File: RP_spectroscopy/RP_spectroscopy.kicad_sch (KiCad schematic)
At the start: 0 parts

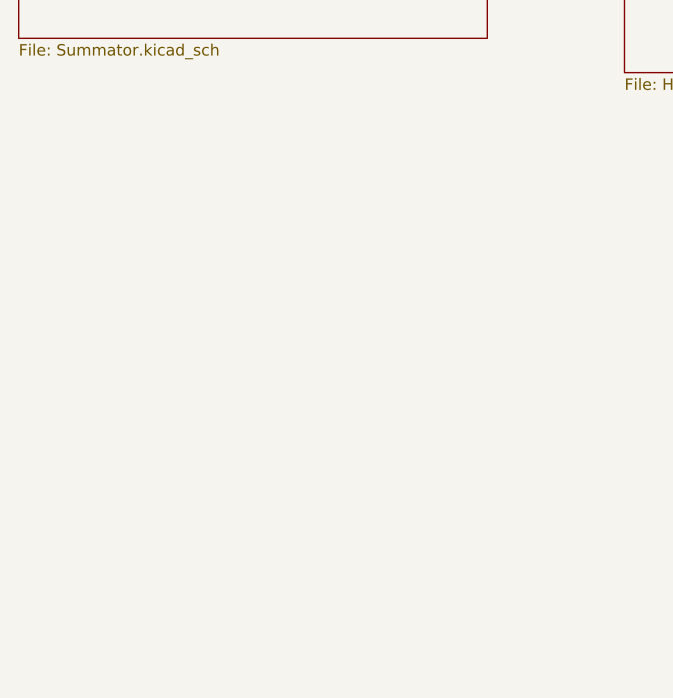
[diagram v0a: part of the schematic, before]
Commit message: Added the VCO schematic and started to draw it.
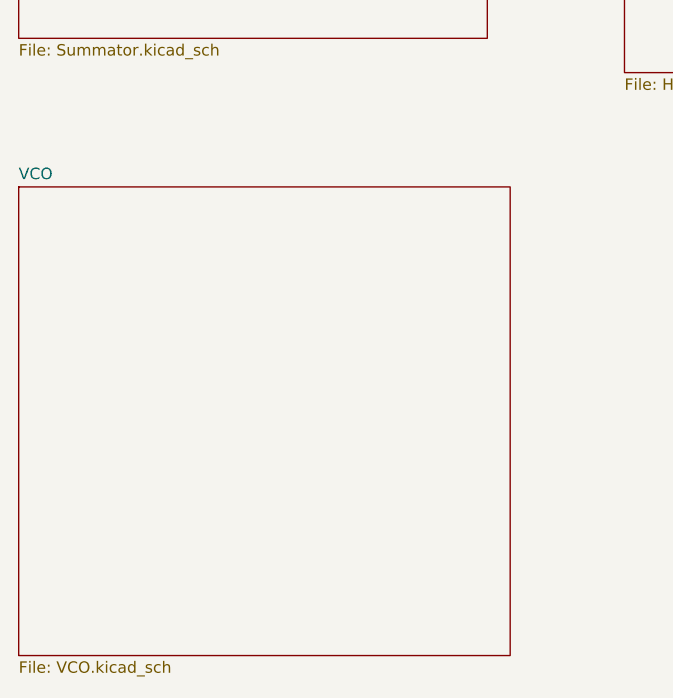
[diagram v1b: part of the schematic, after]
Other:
- added sheet VCO (VCO.kicad_sch)
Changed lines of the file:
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@@
+	)
+	(sheet
+		(at 21.59 88.9)
+		(size 54.61 52.07)
+		(exclude_from_sim no)
+		(in_bom yes)
+		(on_board yes)
+		(dnp no)
+		(fields_autoplaced yes)
+		(stroke
+			(width 0.1524)
+			(type solid)
+		)
+		(fill
+			(color 0 0 0 0.0000)
+		)
+		(property "Sheetname" "VCO"
+			(at 21.59 88.1884 0)
+			(effects
+				(font
+					(size 1.27 1.27)
+				)
+				(justify left bottom)
+			)
+		)
+		(property "Sheetfile" "VCO.kicad_sch"
+			(at 21.59 141.5546 0)
+			(effects
+				(font
+					(size 1.27 1.27)
+				)
+				(justify left top)
+			)
+		)
+		(instances
+			(project "RP_spectroscopy"
+				(path "/dd9ac3ef-6a3a-4df6-b083-1a4e73093ea8"
+					(page "6")
+				)
+			)
+		)
 	)
 	(sheet

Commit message: Deleted the VCO part from the main project
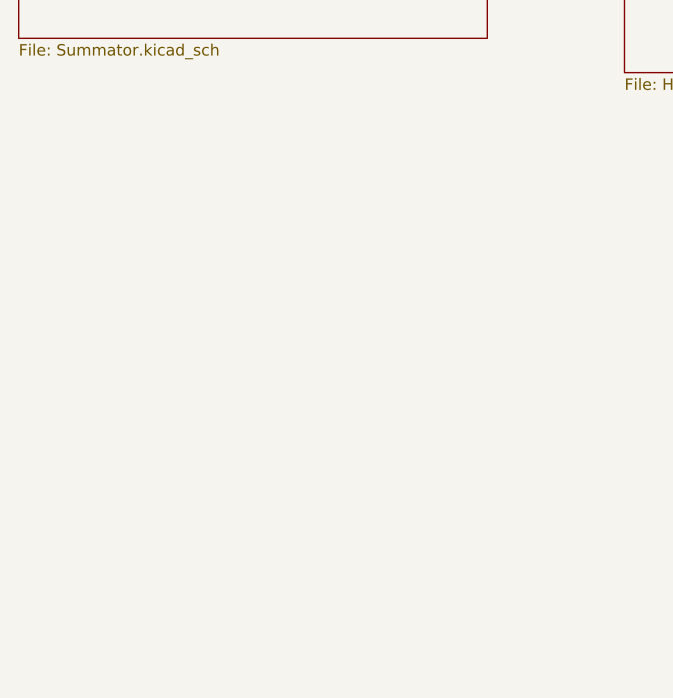
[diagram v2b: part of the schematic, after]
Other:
- removed sheet VCO
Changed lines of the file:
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@@
-	)
-	(sheet
-		(at 21.59 88.9)
-		(size 54.61 52.07)
-		(exclude_from_sim no)
-		(in_bom yes)
-		(on_board yes)
-		(dnp no)
-		(fields_autoplaced yes)
-		(stroke
-			(width 0.1524)
-			(type solid)
-		)
-		(fill
-			(color 0 0 0 0.0000)
-		)
-		(property "Sheetname" "VCO"
-			(at 21.59 88.1884 0)
-			(effects
-				(font
-					(size 1.27 1.27)
-				)
-				(justify left bottom)
-			)
-		)
-		(property "Sheetfile" "VCO.kicad_sch"
-			(at 21.59 141.5546 0)
-			(effects
-				(font
-					(size 1.27 1.27)
-				)
-				(justify left top)
-			)
-		)
-		(instances
-			(project "RP_spectroscopy"
-				(path "/dd9ac3ef-6a3a-4df6-b083-1a4e73093ea8"
-					(page "6")
-				)
-			)
-		)
 	)
 	(sheet
